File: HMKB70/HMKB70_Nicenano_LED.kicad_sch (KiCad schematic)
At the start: 253 parts, among them U1 Nice_Nano_V2

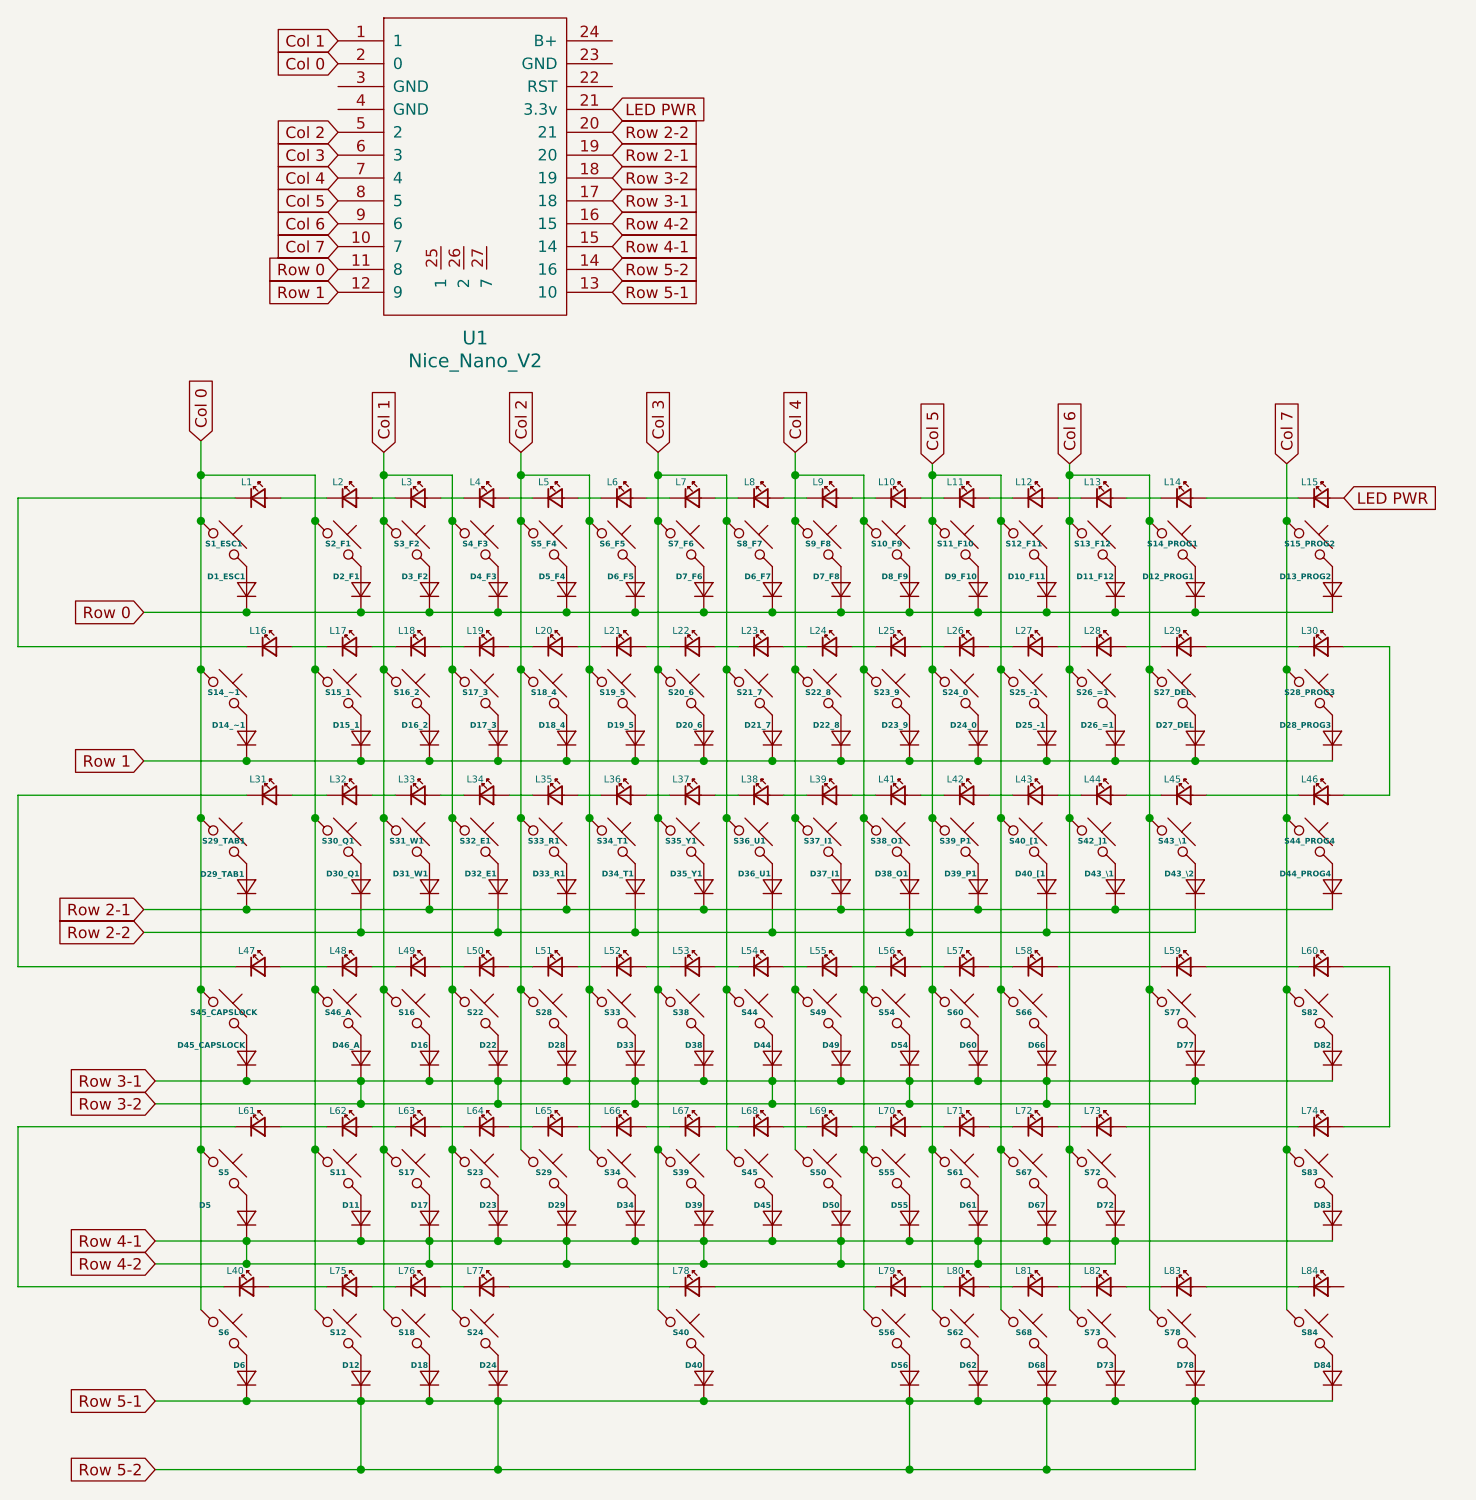
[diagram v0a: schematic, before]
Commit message: 1u footprint fix and misc other
Fixed 1u MX switch footprint, changed LED line to an ugly magenta, fixed LED circuit with current drain.
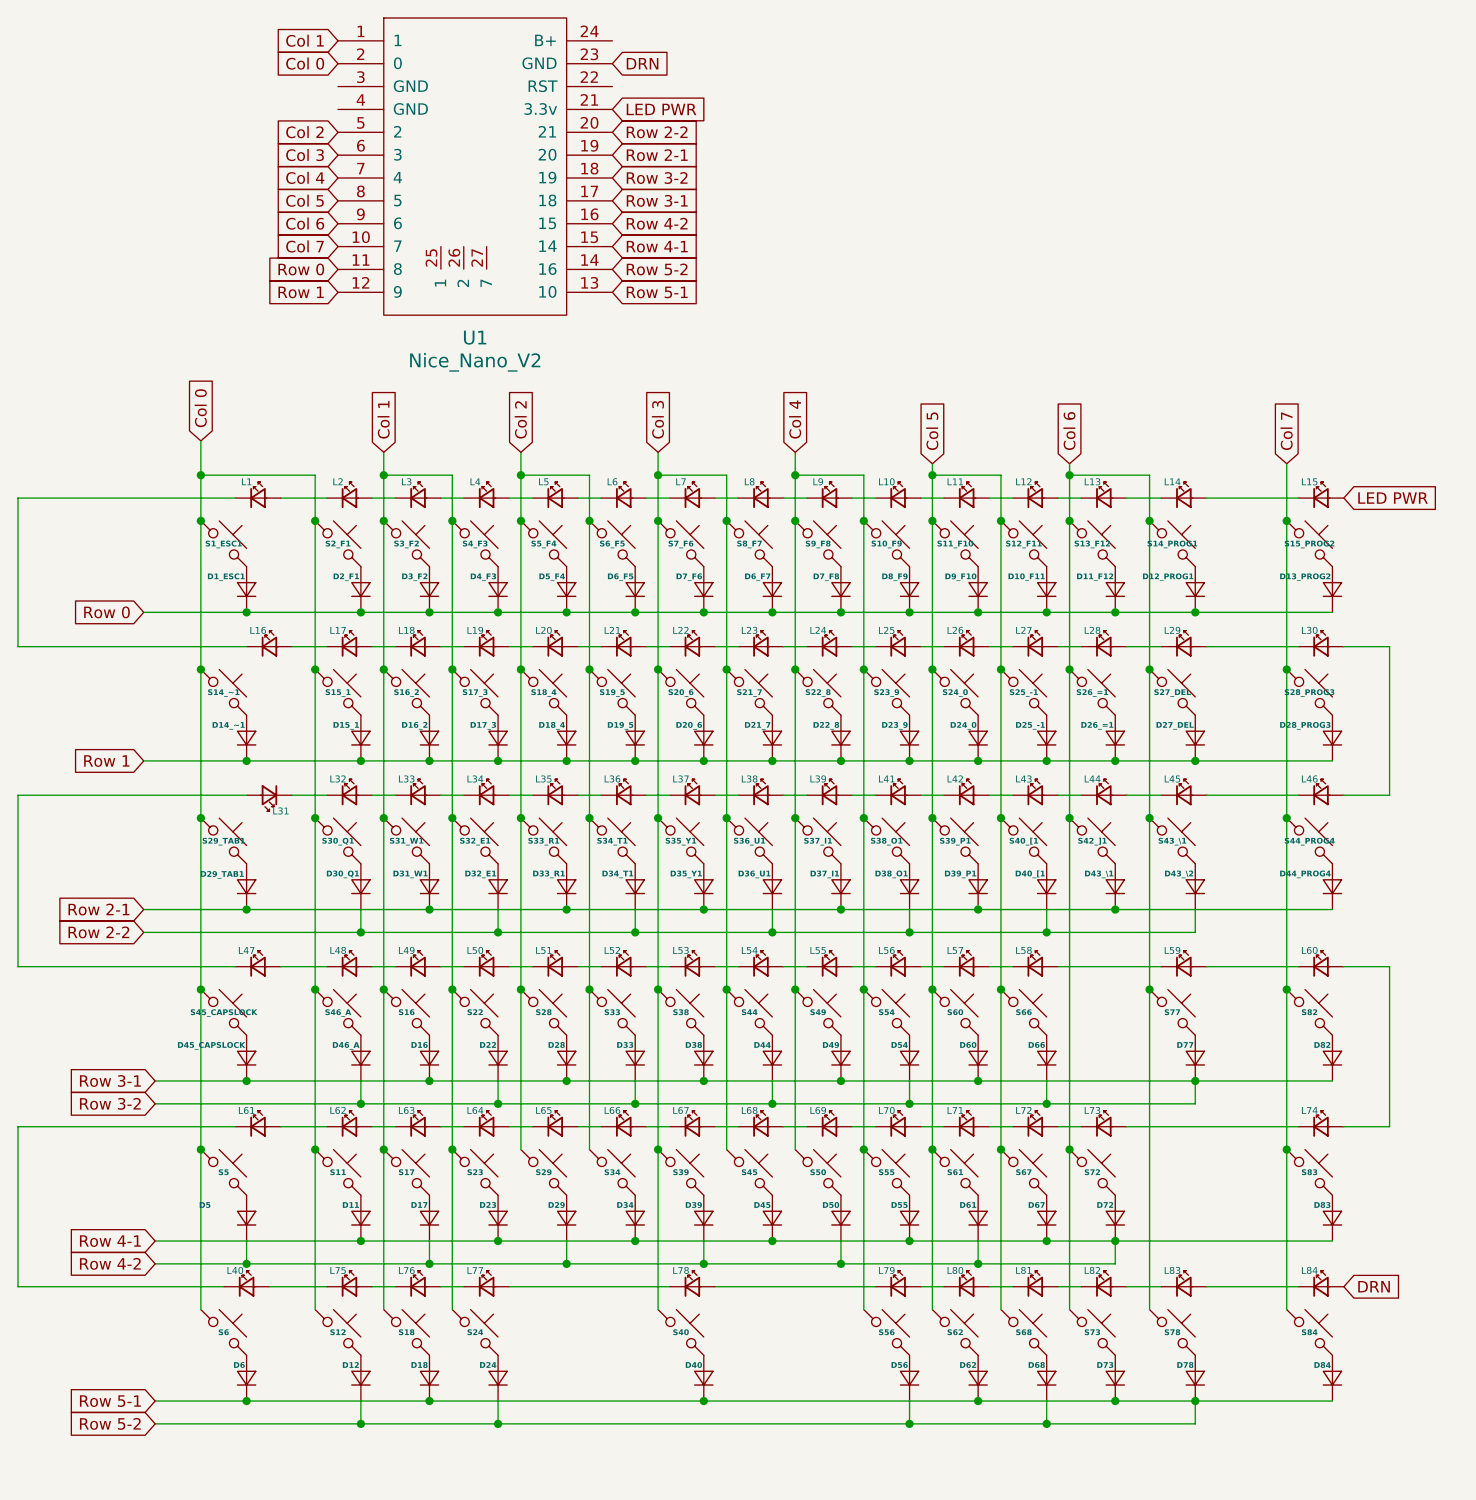
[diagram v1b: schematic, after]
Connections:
- net DRN: now reaches U1.23 (GND)
- net DRN: now also L84.2 (A)
- net at L32.1 (K): now also L31.1 (K); no longer L31.2 (A)
- net at L47.1 (K): now also L31.2 (A); no longer L31.1 (K)
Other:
- moved on the sheet: L31
